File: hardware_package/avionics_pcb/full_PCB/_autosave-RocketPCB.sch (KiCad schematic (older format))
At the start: 72 parts, among them J1 DX07S024XJ1R1100, J2 Micro_SD_Card, J3 Conn_01x03_Female, M1 Motor_Servo_JR, M2 Motor_Servo_JR, Q1 DMG2301L, Q2 DMG2301L, SW1 SW_Push, SW2 SW_Push, U1 STM32F405RGTx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

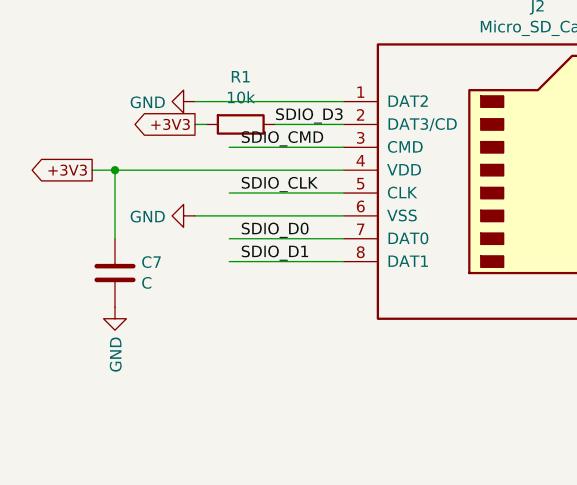
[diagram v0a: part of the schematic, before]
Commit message: Fixed IMU, USB & JR conn fp/p/o conflict, laid out PCB blocks
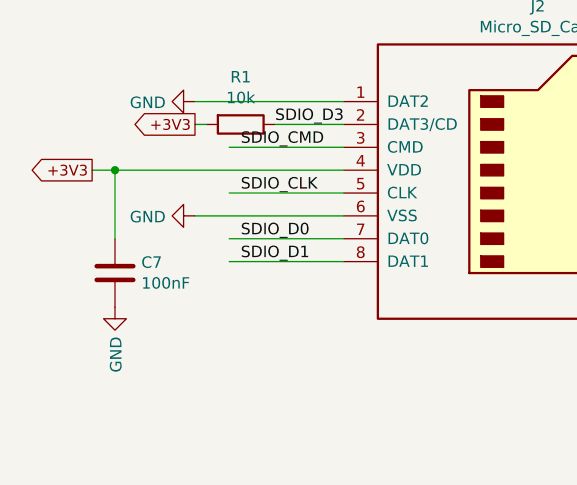
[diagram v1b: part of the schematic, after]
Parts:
- C7: value C -> 100nF
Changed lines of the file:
@@
 Wire Wire Line
 	7550 4700 8000 4700
-$Comp
-L MCU_ST_STM32F4:STM32F405RGTx U1
-U 1 1 5F2C61AB
-P 6850 3600
-F 0 "U1" H 6450 1850 50  0000 C CNN
-F 1 "STM32F405RGTx" H 6800 3700 50  0000 C CNN
-F 2 "Package_QFP:LQFP-64_10x10mm_P0.5mm" H 6250 1900 50  0001 R CNN
-F 3 "http://www.st.com/st-web-ui/static/active/en/resource/technical/document/datasheet/DM00037051.pdf" H 6850 3600 50  0001 C CNN
-	1    6850 3600
-	1    0    0    -1
-$EndComp
 Wire Wire Line
 	7650 3000 7550 3000
@@
 FLASH_MOSI
 Wire Wire Line
-	8600 4050 8600 4200
-Wire Wire Line
 	8450 4200 8600 4200
 $Comp
@@
 	1    0    0    -1
 $EndComp
-Wire Wire Line
-	7550 2000 7850 2000
 Wire Wire Line
 	7550 2100 7850 2100
@@
 P 850 10400
 F 0 "C7" H 965 10446 50  0000 L CNN
-F 1 "C" H 965 10355 50  0000 L CNN
+F 1 "100nF" H 965 10355 50  0000 L CNN
 F 2 "Capacitor_SMD:C_0603_1608Metric" H 888 10250 50  0001 C CNN
 F 3 "~" H 850 10400 50  0001 C CNN
@@
 NoConn ~ 1200 1900
 NoConn ~ 1200 1800
+Wire Wire Line
+	8600 4050 8600 4200
+Wire Wire Line
+	7550 2000 7850 2000
+$Comp
+L MCU_ST_STM32F4:STM32F405RGTx U1
+U 1 1 5F2C61AB
+P 6850 3600
+F 0 "U1" H 6450 1850 50  0000 C CNN
+F 1 "STM32F405RGTx" H 6800 3700 50  0000 C CNN
+F 2 "Package_QFP:LQFP-64_10x10mm_P0.5mm" H 6250 1900 50  0001 R CNN
+F 3 "http://www.st.com/st-web-ui/static/active/en/resource/technical/document/datasheet/DM00037051.pdf" H 6850 3600 50  0001 C CNN
+	1    6850 3600
+	1    0    0    -1
+$EndComp
 $EndSCHEMATC

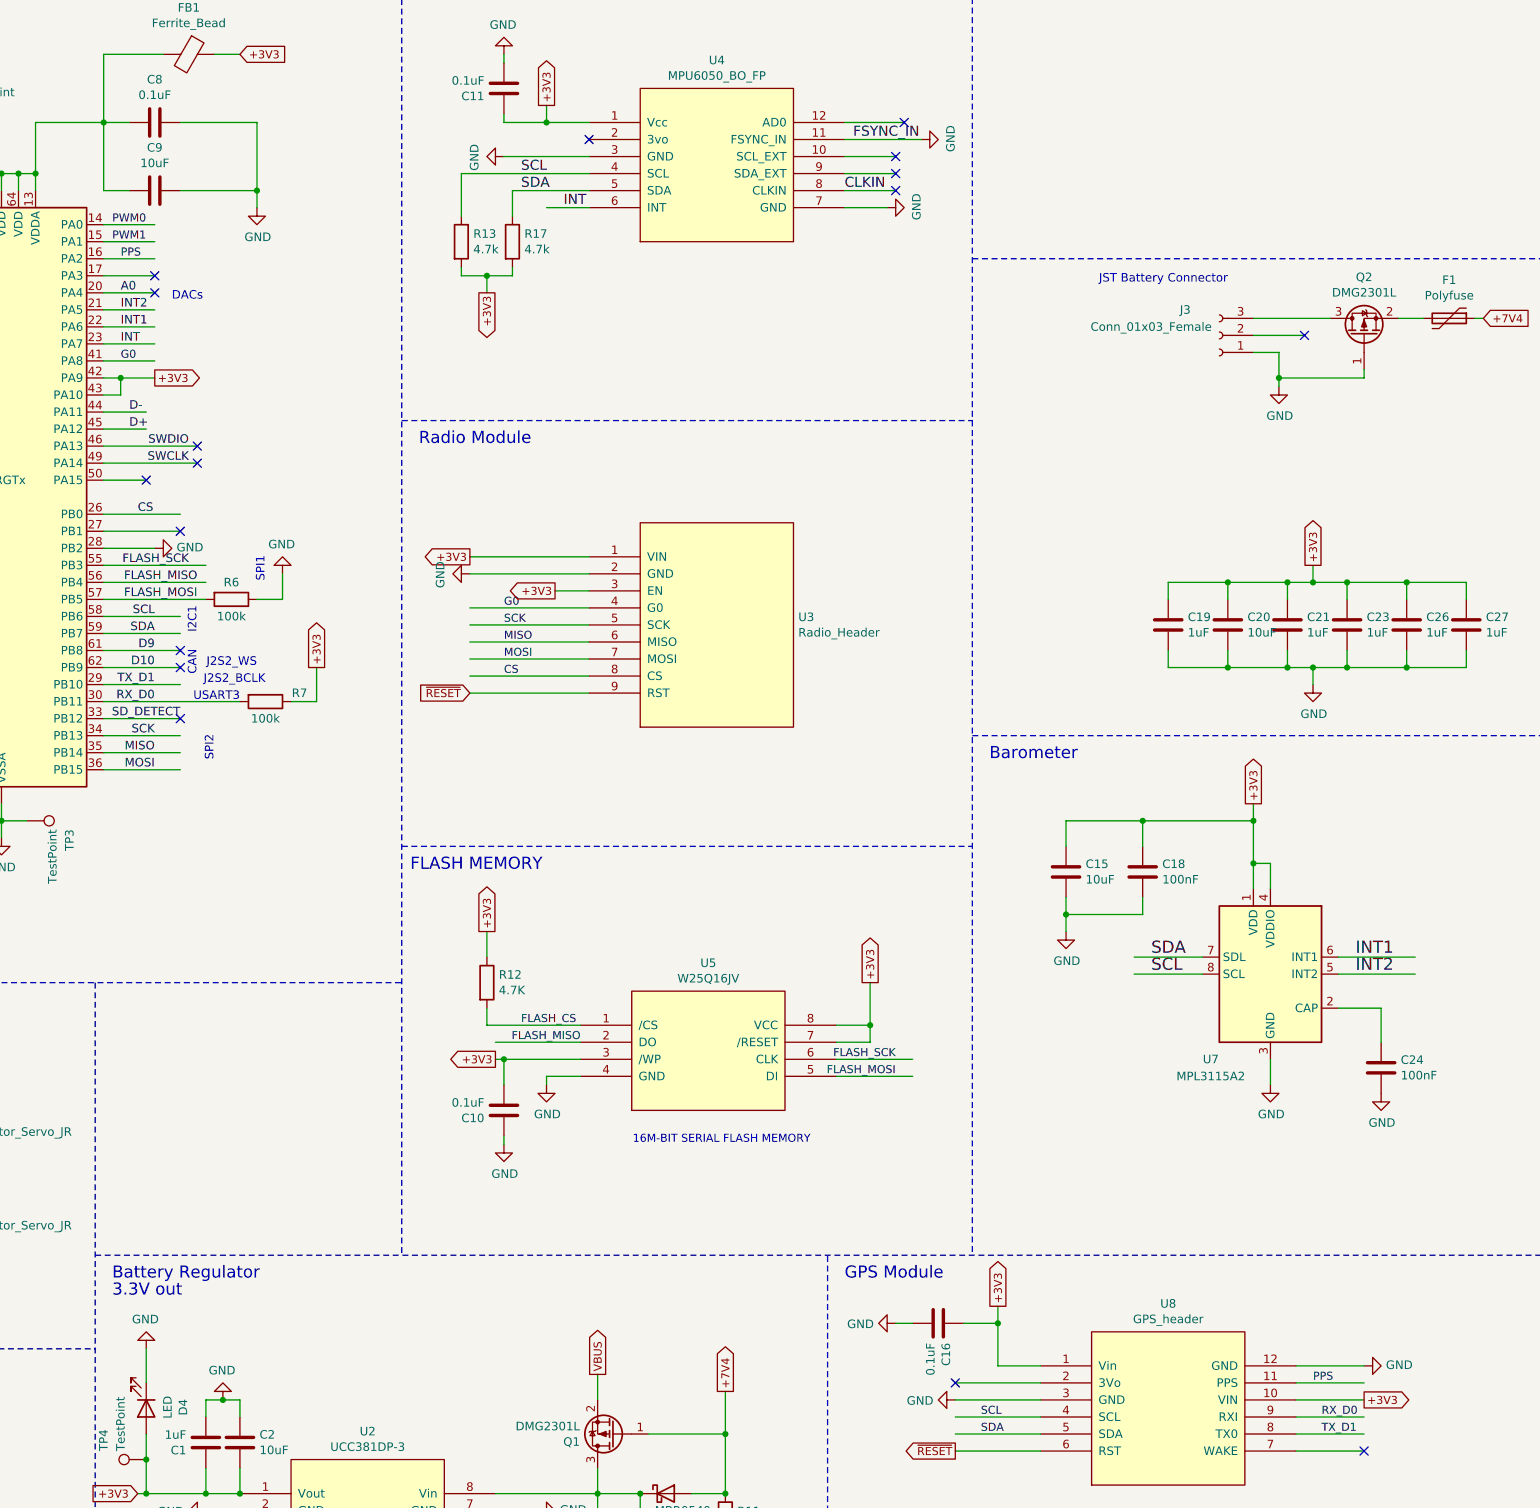
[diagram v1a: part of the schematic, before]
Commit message: Modified to 4 layer PCB, laid out 6V and 3V3 regulators
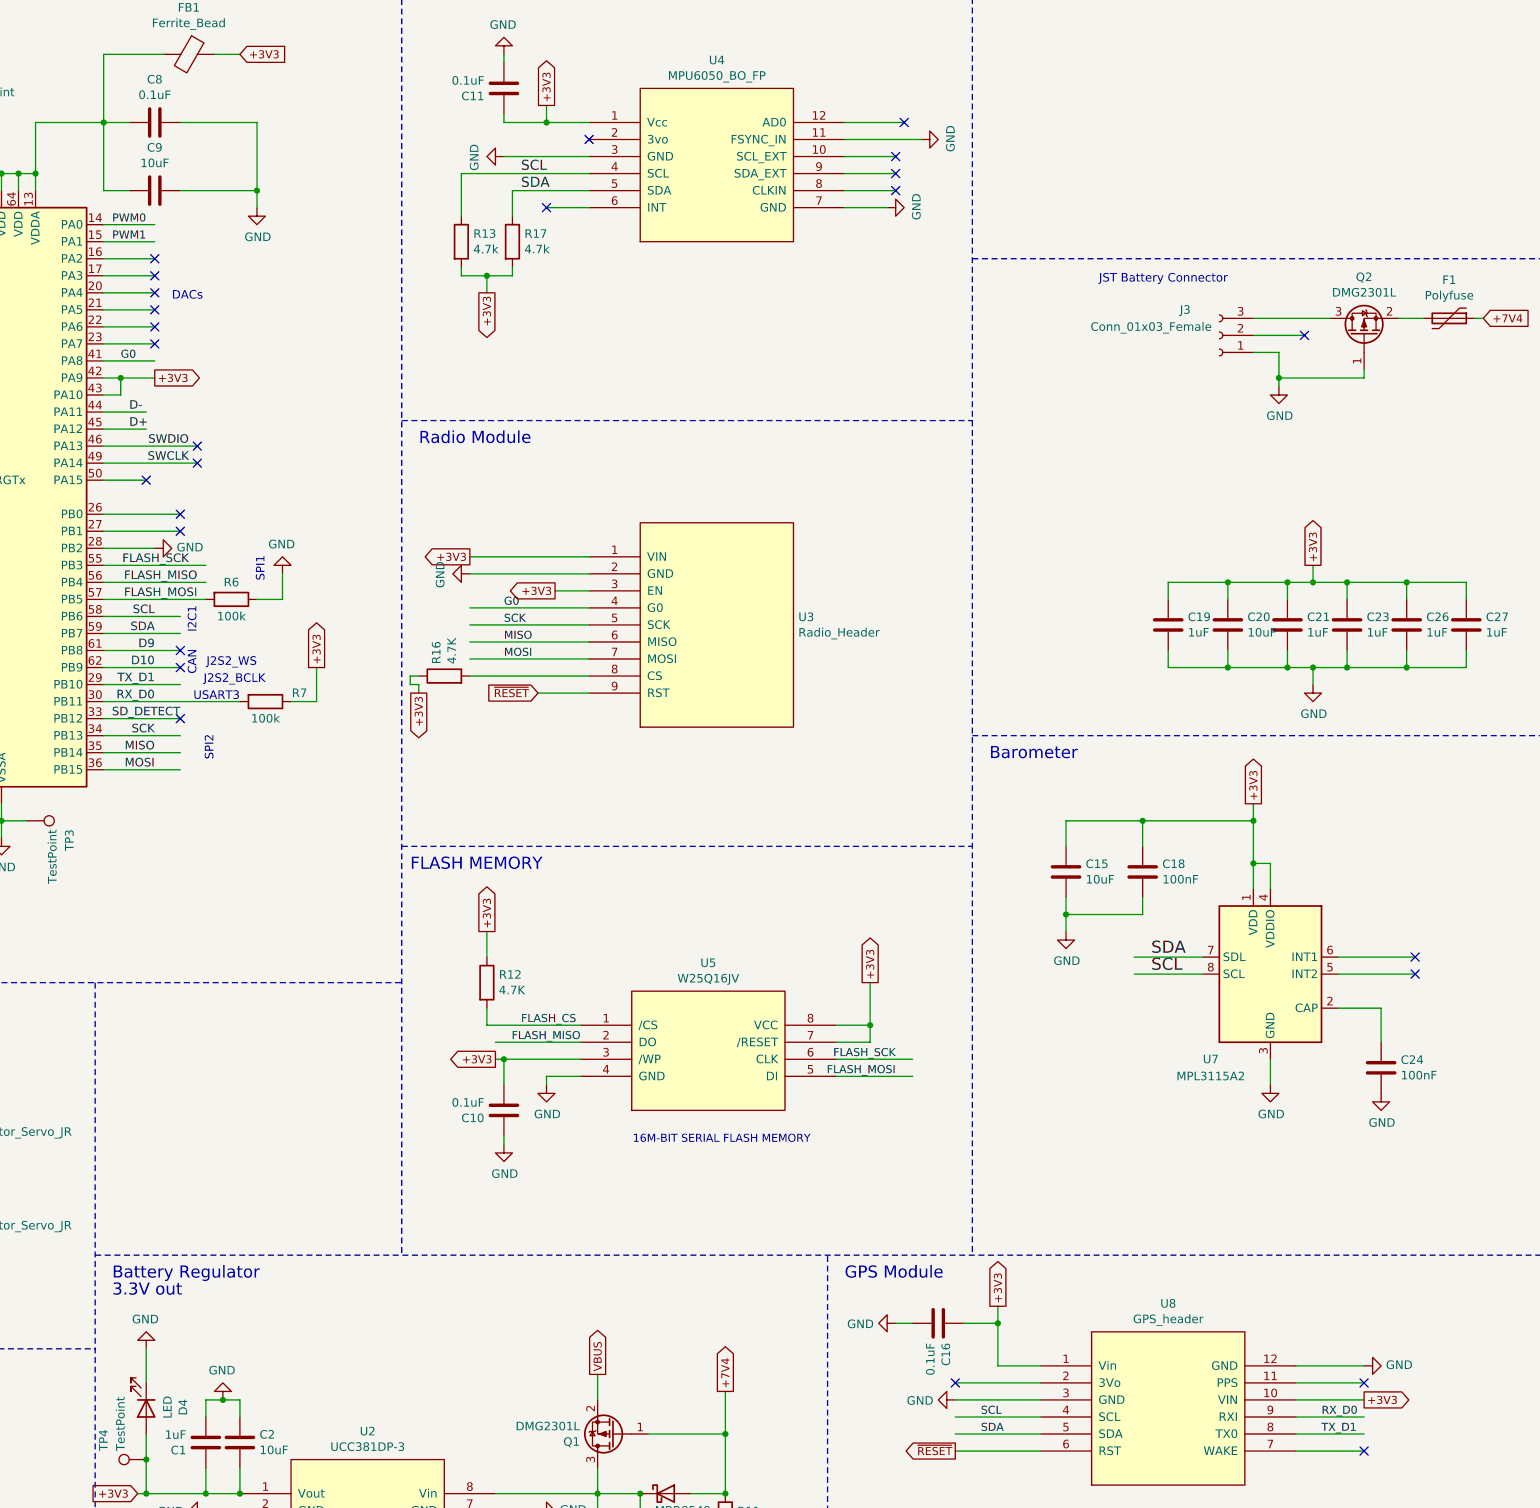
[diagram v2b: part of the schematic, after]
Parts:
- added R16: 4.7K, Resistor_SMD:R_0603_1608Metric, symbol Device:R
- J1: footprint JAE_DX07S024XJ1R1100 -> DX07S024XJ1R1100:JAE_DX07S024XJ1R1100
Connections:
- net labels removed: A0, CLKIN, CS, FSYNC_IN, INT, INT1, INT2, PPS
- wire segments 360 -> 364
- no-connect marks 42 -> 51
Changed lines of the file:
@@
 Text Label 5850 2200 0    50   ~ 0
 BOOT0
-Text Label 7650 2400 0    50   ~ 0
-A0
-Text Label 7650 2500 0    50   ~ 0
-INT2
-Text Label 7650 2600 0    50   ~ 0
-INT1
 Text Notes 7950 2450 0    50   ~ 0
 DACs
@@
 Wire Wire Line
 	7650 2900 7650 3000
-Text Label 7650 2700 0    50   ~ 0
-INT
 Wire Wire Line
 	6850 5500 6950 5500
@@
 Wire Notes Line
 	11800 9950 11800 8050
-Text Label 10250 1900 0    59   ~ 0
-INT
-Text Label 11950 1500 0    59   ~ 0
-FSYNC_IN
-Text Label 11900 1800 0    59   ~ 0
-CLKIN
 Text Label 10000 1700 0    59   ~ 0
 SCL
@@
 Wire Wire Line
 	7550 3700 8000 3700
-Text Label 7750 3700 0    50   ~ 0
-CS
 $Comp
 L power:GND #PWR030
@@
 Wire Wire Line
 	14800 6400 15250 6400
-Text Label 14900 6300 0    71   ~ 0
-INT1
-Text Label 14900 6400 0    71   ~ 0
-INT2
 Text Notes 12750 5150 0    71   ~ 0
 Barometer\n
@@
 Wire Wire Line
 	10400 4650 9700 4650
-Wire Wire Line
-	10400 4750 9700 4750
 $Comp
 L power:GND #PWR0102
@@
 Wire Wire Line
 	7550 2200 7850 2200
-Text Label 7650 2200 0    47   ~ 0
-PPS
-Text Label 14650 8800 0    47   ~ 0
-PPS
 Text Label 14700 9000 0    47   ~ 0
 RX_D0
@@
 Wire Wire Line
 	7550 2800 7850 2800
-Text Label 7650 2800 0    47   ~ 0
-G0
-Text Label 9900 4250 0    47   ~ 0
-G0
 Text Label 9900 4350 0    47   ~ 0
 SCK
@@
 Text Label 9900 4550 0    47   ~ 0
 MOSI
-Text Label 9900 4650 0    47   ~ 0
-CS
 Text Notes 11900 8200 0    71   ~ 0
 GPS Module
@@
 Text GLabel 12550 9200 0    47   Output ~ 0
 ~RESET~
-Text GLabel 9700 4750 0    47   Input ~ 0
+Text GLabel 10100 4750 0    47   Input ~ 0
 ~RESET~
 NoConn ~ 7800 3500
@@
 F 0 "J1" H 2150 2965 50  0000 C CNN
 F 1 "DX07S024XJ1R1100" H 2150 2874 50  0000 C CNN
-F 2 "JAE_DX07S024XJ1R1100" H 2150 2000 50  0001 L BNN
+F 2 "DX07S024XJ1R1100:JAE_DX07S024XJ1R1100" H 2150 2000 50  0001 L BNN
 F 3 "JAE" H 2150 2000 50  0001 L BNN
 F 4 "3.34mm" H 2150 2000 50  0001 L BNN "Field4"
@@
 	1    0    0    -1
 $EndComp
+NoConn ~ 10150 1900
+$Comp
+L Device:R R16
+U 1 1 608B0935
+P 9550 4650
+F 0 "R16" H 9620 4696 50  0000 L CNN
+F 1 "4.7K" H 9620 4605 50  0000 L CNN
+F 2 "Resistor_SMD:R_0603_1608Metric" V 9480 4650 50  0001 C CNN
+F 3 "~" H 9550 4650 50  0001 C CNN
+	1    9550 4650
+	0    -1   -1   0
+$EndComp
+Wire Wire Line
+	10100 4750 10400 4750
+Wire Wire Line
+	9400 4650 9350 4650
+Wire Wire Line
+	9350 4650 9350 4700
+Text GLabel 9400 4750 3    47   Output ~ 0
++3V3
+NoConn ~ 8000 3700
+NoConn ~ 7850 2700
+Wire Wire Line
+	9400 4750 9400 4700
+Wire Wire Line
+	9400 4700 9350 4700
+NoConn ~ 7850 2200
+NoConn ~ 14950 8800
+Text Label 7650 2800 0    47   ~ 0
+G0
+Text Label 9900 4250 0    47   ~ 0
+G0
+NoConn ~ 15250 6300
+NoConn ~ 15250 6400
+NoConn ~ 7850 2500
+NoConn ~ 7850 2600
 $EndSCHEMATC
